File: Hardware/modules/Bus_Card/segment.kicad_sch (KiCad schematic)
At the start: 10 parts, among them U13 SA39-11EWA, U14 GAL16V8

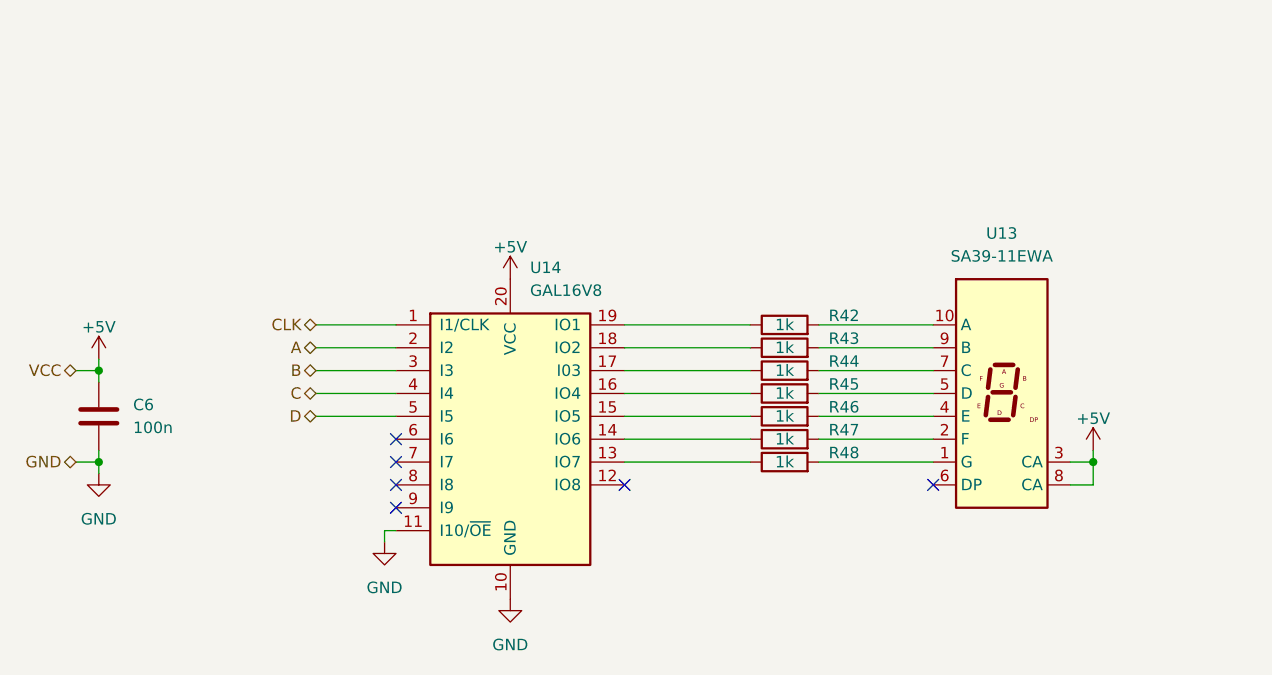
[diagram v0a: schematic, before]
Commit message: Bus Card Update & GAL code compilation
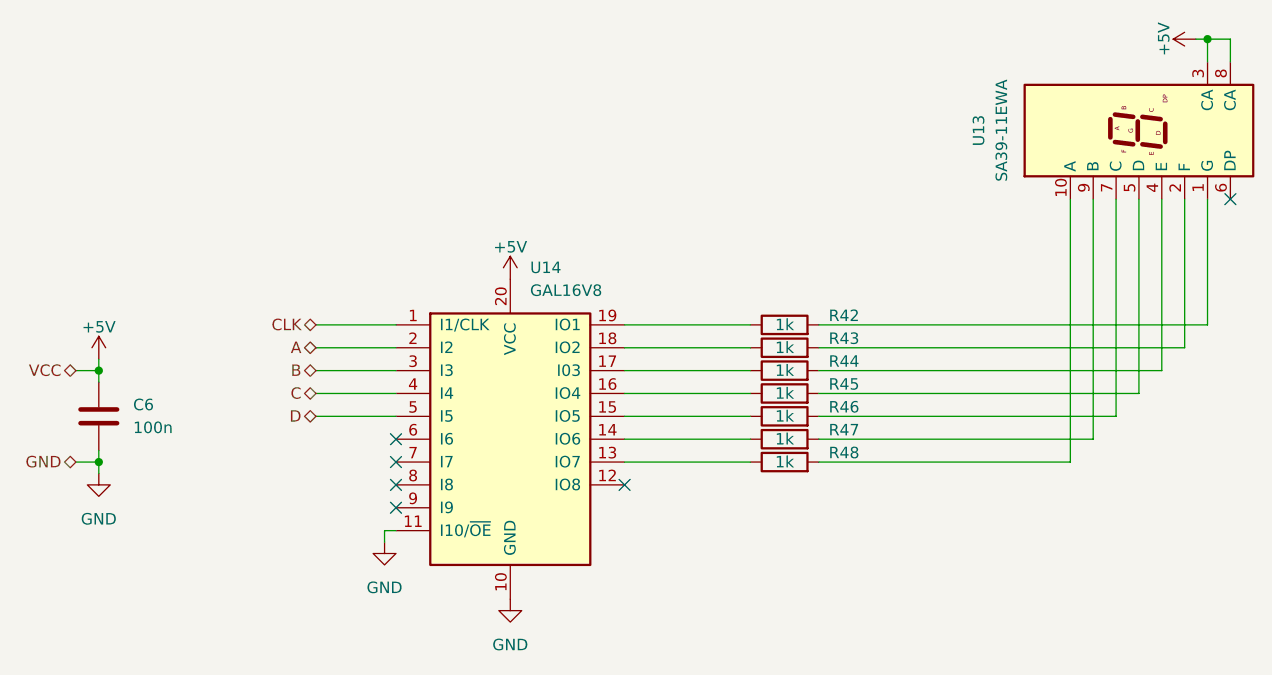
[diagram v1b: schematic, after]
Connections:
- net at R46.2: now also U13.7 (C); no longer U13.4 (E)
- net at R47.2: now also U13.9 (B); no longer U13.2 (F)
- net at R43.2: now also U13.2 (F); no longer U13.9 (B)
- net at R48.2: now also U13.10 (A); no longer U13.1 (G)
- net at R42.2: now also U13.1 (G); no longer U13.10 (A)
- net at R44.2: now also U13.4 (E); no longer U13.7 (C)
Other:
- moved on the sheet: U13
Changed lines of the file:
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@@
 	)
 	(junction
-		(at 179.07 92.71)
+		(at 191.77 45.72)
 		(diameter 0)
 		(color 0 0 0 0)
@@
 	)
 	(no_connect
-		(at 161.29 95.25)
+		(at 194.31 63.5)
 	)
 	(wire
@@
 	(wire
 		(pts
-			(xy 179.07 92.71) (xy 179.07 95.25)
+			(xy 191.77 45.72) (xy 194.31 45.72)
 		)
 		(stroke
@@
 	(wire
 		(pts
-			(xy 179.07 91.44) (xy 179.07 92.71)
+			(xy 190.5 45.72) (xy 191.77 45.72)
+		)
+		(stroke
+			(width 0)
+			(type default)
+		)
+	)
+	(wire
+		(pts
+			(xy 181.61 87.63) (xy 181.61 63.5)
+		)
+		(stroke
+			(width 0)
+			(type default)
+		)
+	)
+	(wire
+		(pts
+			(xy 179.07 90.17) (xy 179.07 63.5)
 		)
 		(stroke
@@
 	(wire
 		(pts
-			(xy 148.59 90.17) (xy 161.29 90.17)
+			(xy 191.77 77.47) (xy 191.77 63.5)
 		)
 		(stroke
@@
 	(wire
 		(pts
+			(xy 189.23 80.01) (xy 189.23 63.5)
+		)
+		(stroke
+			(width 0)
+			(type default)
+		)
+	)
+	(wire
+		(pts
+			(xy 148.59 92.71) (xy 176.53 92.71)
+		)
+		(stroke
+			(width 0)
+			(type default)
+		)
+	)
+	(wire
+		(pts
 			(xy 68.58 82.55) (xy 68.58 83.82)
 		)
@@
 	(wire
 		(pts
+			(xy 148.59 87.63) (xy 181.61 87.63)
+		)
+		(stroke
+			(width 0)
+			(type default)
+		)
+	)
+	(wire
+		(pts
+			(xy 184.15 85.09) (xy 184.15 63.5)
+		)
+		(stroke
+			(width 0)
+			(type default)
+		)
+	)
+	(wire
+		(pts
 			(xy 68.58 93.98) (xy 68.58 92.71)
 		)
@@
 	(wire
 		(pts
+			(xy 148.59 80.01) (xy 189.23 80.01)
+		)
+		(stroke
+			(width 0)
+			(type default)
+		)
+	)
+	(wire
+		(pts
+			(xy 148.59 85.09) (xy 184.15 85.09)
+		)
+		(stroke
+			(width 0)
+			(type default)
+		)
+	)
+	(wire
+		(pts
 			(xy 140.97 85.09) (xy 127 85.09)
 		)
@@
 	(wire
 		(pts
-			(xy 148.59 82.55) (xy 161.29 82.55)
+			(xy 176.53 92.71) (xy 176.53 63.5)
 		)
 		(stroke
@@
 	(wire
 		(pts
+			(xy 148.59 90.17) (xy 179.07 90.17)
+		)
+		(stroke
+			(width 0)
+			(type default)
+		)
+	)
+	(wire
+		(pts
 			(xy 68.58 92.71) (xy 66.04 92.71)
 		)
@@
 	(wire
 		(pts
-			(xy 148.59 92.71) (xy 161.29 92.71)
-		)
-		(stroke
-			(width 0)
-			(type default)
-		)
-	)
-	(wire
-		(pts
-			(xy 148.59 87.63) (xy 161.29 87.63)
-		)
-		(stroke
-			(width 0)
-			(type default)
-		)
-	)
-	(wire
-		(pts
 			(xy 140.97 80.01) (xy 127 80.01)
 		)
@@
 	(wire
 		(pts
-			(xy 179.07 95.25) (xy 176.53 95.25)
-		)
-		(stroke
-			(width 0)
-			(type default)
-		)
-	)
-	(wire
-		(pts
-			(xy 148.59 85.09) (xy 161.29 85.09)
-		)
-		(stroke
-			(width 0)
-			(type default)
-		)
-	)
-	(wire
-		(pts
-			(xy 148.59 80.01) (xy 161.29 80.01)
+			(xy 148.59 77.47) (xy 191.77 77.47)
+		)
+		(stroke
+			(width 0)
+			(type default)
+		)
+	)
+	(wire
+		(pts
+			(xy 194.31 45.72) (xy 194.31 48.26)
 		)
 		(stroke
@@
 	(wire
 		(pts
-			(xy 176.53 92.71) (xy 179.07 92.71)
-		)
-		(stroke
-			(width 0)
-			(type default)
-		)
-	)
-	(wire
-		(pts
-			(xy 148.59 77.47) (xy 161.29 77.47)
+			(xy 191.77 48.26) (xy 191.77 45.72)
 		)
 		(stroke
@@
 		(pts
 			(xy 92.71 87.63) (xy 101.6 87.63)
+		)
+		(stroke
+			(width 0)
+			(type default)
+		)
+	)
+	(wire
+		(pts
+			(xy 186.69 82.55) (xy 186.69 63.5)
+		)
+		(stroke
+			(width 0)
+			(type default)
+		)
+	)
+	(wire
+		(pts
+			(xy 148.59 82.55) (xy 186.69 82.55)
 		)
 		(stroke
@@
 	(symbol
 		(lib_id "power:+5V")
-		(at 179.07 91.44 0)
+		(at 190.5 45.72 90)
 		(unit 1)
 		(exclude_from_sim no)
@@
 		(dnp no)
 		(property "Reference" "#PWR01035"
-			(at 179.07 95.25 0)
+			(at 194.31 45.72 0)
 			(effects
 				(font
@@
 		)
 		(property "Value" "+5V"
-			(at 179.07 87.884 0)
+			(at 186.944 45.72 0)
 			(effects
 				(font
@@
 		)
 		(property "Footprint" ""
-			(at 179.07 91.44 0)
+			(at 190.5 45.72 0)
 			(effects
 				(font
@@
 		)
 		(property "Datasheet" ""
-			(at 179.07 91.44 0)
+			(at 190.5 45.72 0)
 			(effects
 				(font
@@
 		)
 		(property "Description" "Power symbol creates a global label with name \"+5V\""
-			(at 179.07 91.44 0)
+			(at 190.5 45.72 0)
 			(effects
 				(font
@@
 	(symbol
 		(lib_id "Display_Character:SA39-11EWA")
-		(at 168.91 85.09 0)
+		(at 184.15 55.88 90)
 		(unit 1)
 		(exclude_from_sim no)
@@
 		(fields_autoplaced yes)
 		(property "Reference" "U13"
-			(at 168.91 67.31 0)
+			(at 166.37 55.88 0)
 			(effects
 				(font
@@
 		)
 		(property "Value" "SA39-11EWA"
-			(at 168.91 69.85 0)
+			(at 168.91 55.88 0)
 			(effects
 				(font
@@
 		)
 		(property "Footprint" "Display_7Segment:Sx39-1xxxxx"
-			(at 168.91 99.06 0)
+			(at 198.12 55.88 0)
 			(effects
 				(font
@@
 		)
 		(property "Datasheet" "http://www.kingbrightusa.com/images/catalog/SPEC/sa39-11ewa.pdf"
-			(at 168.91 85.09 0)
+			(at 184.15 55.88 0)
 			(effects
 				(font
@@
 		)
 		(property "Description" "Single digit 7 segment display, high efficiency red, common anode"
-			(at 168.91 85.09 0)
-			(effects
-				(font
+			(at 184.15 55.88 0)
+			(effects
+				(font
